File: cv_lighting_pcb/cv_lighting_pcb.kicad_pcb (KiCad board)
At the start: 2 copper layers, 83.8 x 78.7 mm, 27 parts, among them Q1 2N3906, U1 Current Driver, U2 Camera Input, U3 VO617A, U4 Barrel Jack

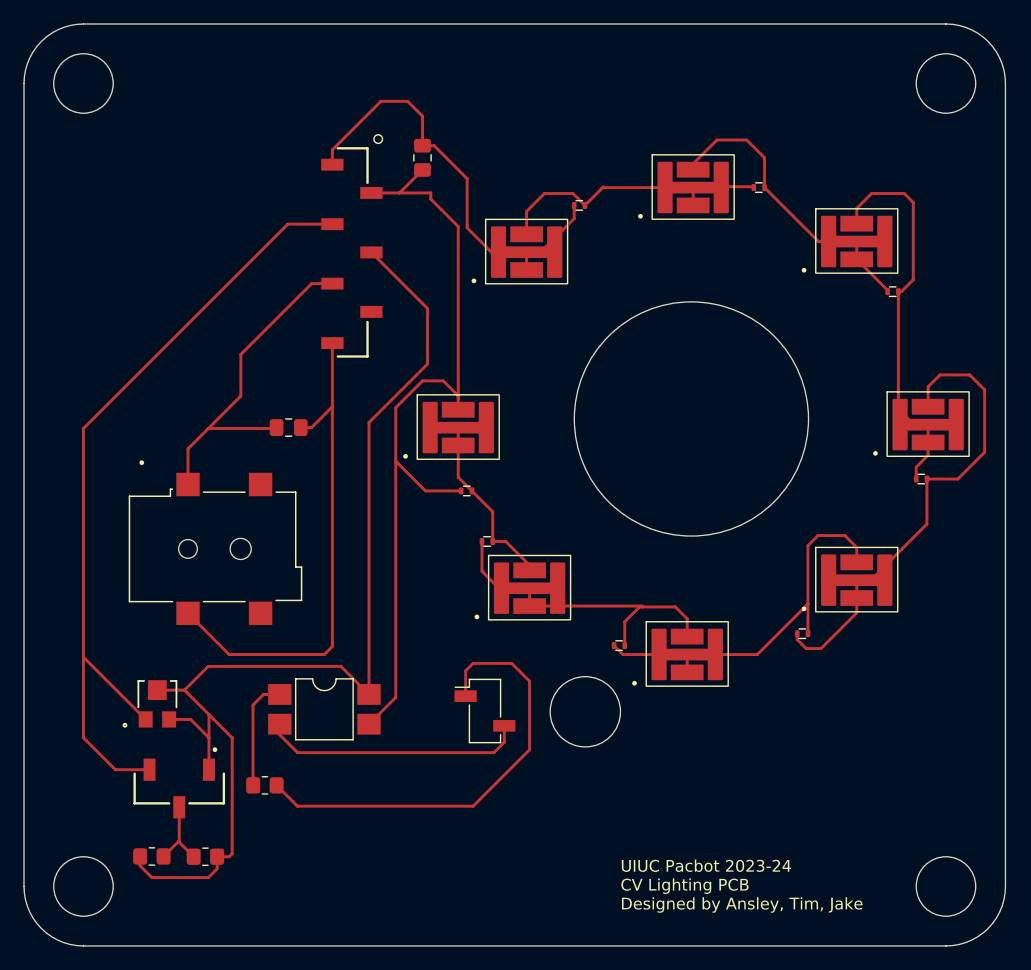
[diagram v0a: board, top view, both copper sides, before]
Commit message: more changes to lighting pcb
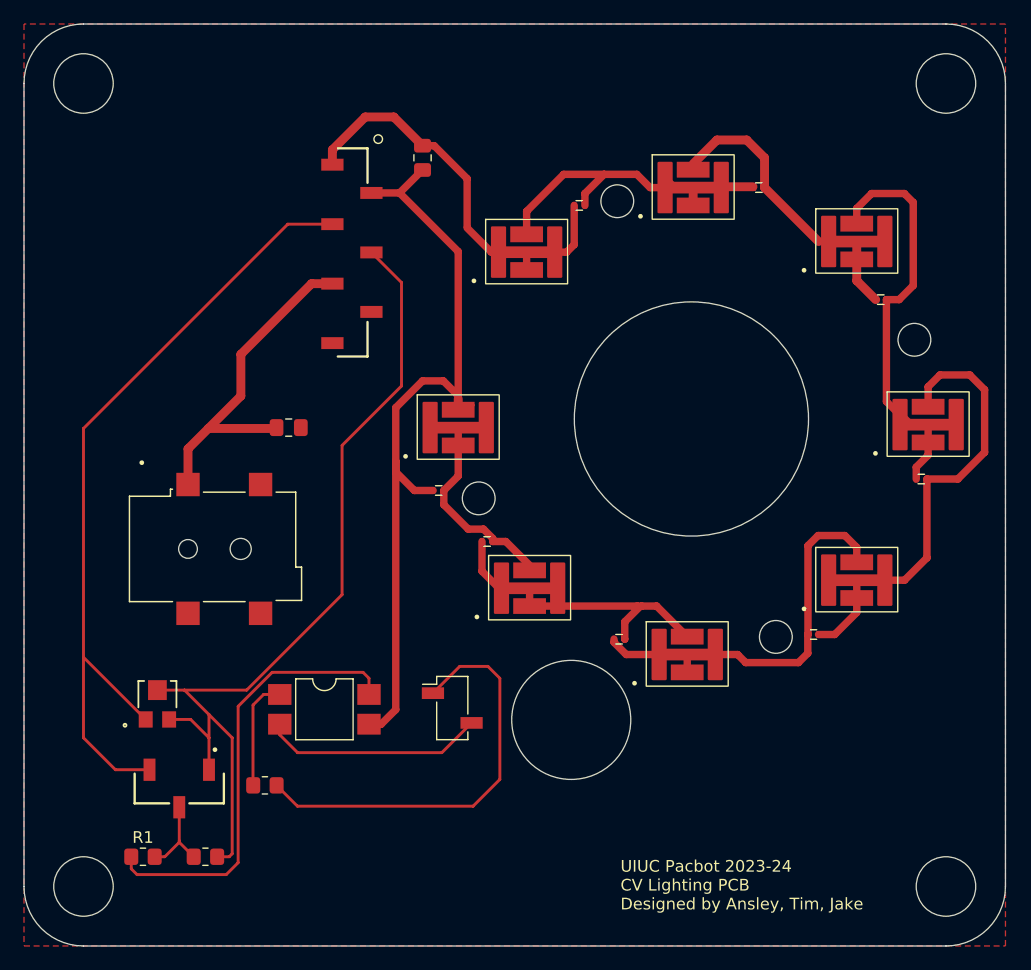
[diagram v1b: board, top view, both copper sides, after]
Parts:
- R3: value 1K -> 200
- moved D12 7.94 mm to (166.5, 104.3), turned to 180 degrees
- moved U2 2.81 mm to (135.6, 106.7)
- moved D15 2.40 mm to (134.5, 92.0)
- moved D10 1.23 mm to (172.3, 67.9)
- moved R1 0.76 mm to (109.2, 119.4)
- moved D13 0.55 mm to (149.9, 96.9)
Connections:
- R1 pad 1: Net-(Q1-E) -> Net-(R1-Pad1)
- U3 pad 4: Net-(Q1-E) -> Net-(R1-Pad1)
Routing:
- net GND: track 43.4 -> 0.00 mm
- net Net-(R1-Pad1): track 0.00 -> 38.1 mm
- net Net-(Q1-E): track 96.7 -> 77.4 mm
- net Net-(D1-K): track 24.3 -> 30.4 mm
- net Net-(U2-PWM_GND): track 22.5 -> 19.0 mm
- net Net-(D10-A): track 33.4 -> 36.9 mm
- net Net-(U2-PWM_Input): track 38.7 -> 36.5 mm
- net Net-(D15-A): track 70.7 -> 68.8 mm
- net Net-(D14-A): track 15.4 -> 17.1 mm
- net Net-(D13-A): track 28.2 -> 27.2 mm
- net Net-(D12-A): track 33.9 -> 34.8 mm
- net Net-(Q1-B): track 6.63 -> 7.35 mm
- added copper zone on F.Cu, net GND
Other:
- outline, holes or cut-outs redrawn

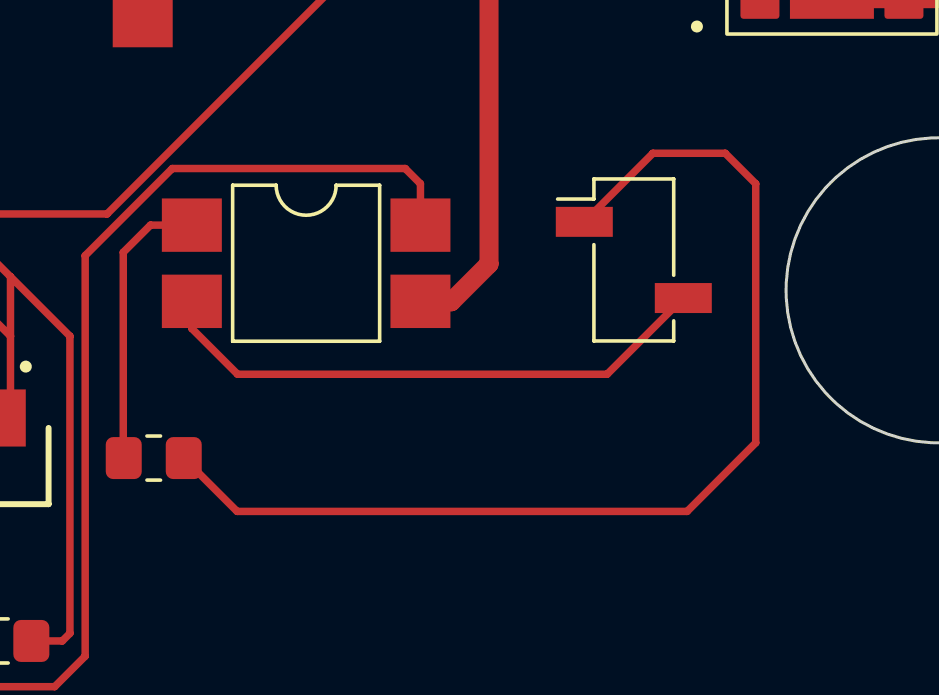
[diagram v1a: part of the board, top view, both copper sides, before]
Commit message: more changes to lighting pcb
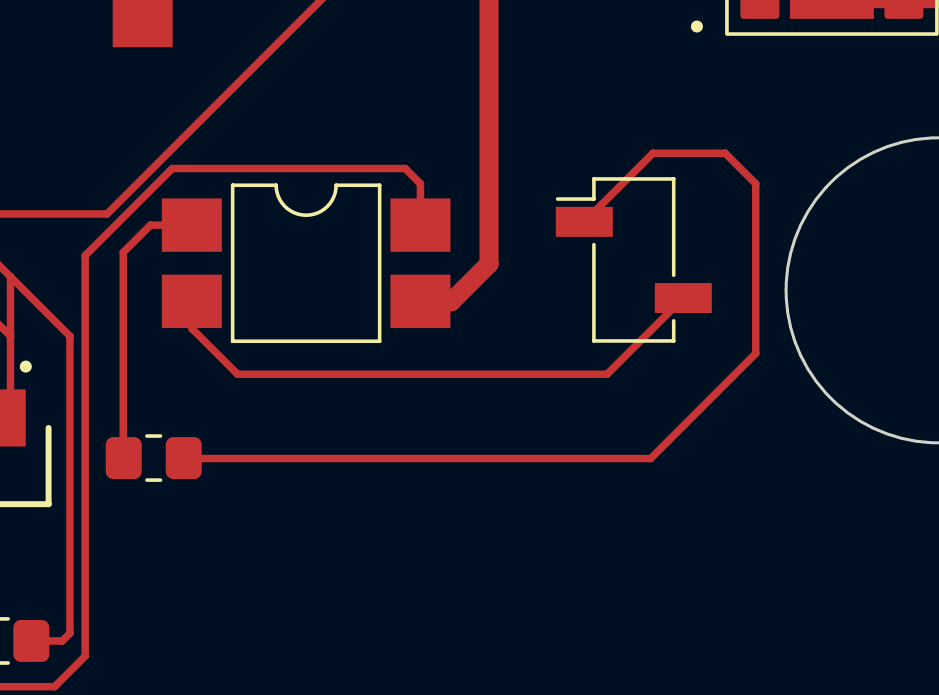
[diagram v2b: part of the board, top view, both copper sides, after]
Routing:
- net Net-(U2-PWM_Input): track 36.5 -> 33.3 mm
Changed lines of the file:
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@@
     (effects (font (size 1 1) (thickness 0.15)) (justify left bottom))
   )
-  (gr_text "hole for wire from camera to pcb\n\n" (at 149.86 116.332) (layer "F.Fab")
+  (gr_text "hole for wire from camera to pcb\n\n" (at 141.9 116.4) (layer "F.Fab")
     (effects (font (size 1 1) (thickness 0.15)) (justify left bottom))
   )
@@
   (segment (start 118.618 113.268) (end 118.634 113.284) (width 0.25) (layer "F.Cu") (net 14))
   (segment (start 119.5245 105.5195) (end 118.618 106.426) (width 0.25) (layer "F.Cu") (net 14))
-  (segment (start 139.7 112.776) (end 137.414 115.062) (width 0.25) (layer "F.Cu") (net 15))
-  (segment (start 139.7 104.14) (end 139.7 112.776) (width 0.25) (layer "F.Cu") (net 15))
   (segment (start 138.684 103.124) (end 139.7 104.14) (width 0.25) (layer "F.Cu") (net 15))
+  (segment (start 136.2 113.3) (end 120.65 113.3) (width 0.25) (layer "F.Cu") (net 15))
+  (segment (start 120.65 113.3) (end 120.634 113.284) (width 0.25) (layer "F.Cu") (net 15))
+  (segment (start 139.7 109.8) (end 136.2 113.3) (width 0.25) (layer "F.Cu") (net 15))
+  (segment (start 139.7 104.14) (end 139.7 109.8) (width 0.25) (layer "F.Cu") (net 15))
+  (segment (start 133.986 105.41) (end 136.272 103.124) (width 0.25) (layer "F.Cu") (net 15))
   (segment (start 136.272 103.124) (end 138.684 103.124) (width 0.25) (layer "F.Cu") (net 15))
-  (segment (start 137.414 115.062) (end 122.412 115.062) (width 0.25) (layer "F.Cu") (net 15))
-  (segment (start 133.986 105.41) (end 136.272 103.124) (width 0.25) (layer "F.Cu") (net 15))
-  (segment (start 122.412 115.062) (end 120.634 113.284) (width 0.25) (layer "F.Cu") (net 15))
   (segment (start 120.904 108.966) (end 122.428 110.49) (width 0.25) (layer "F.Cu") (net 17))
   (segment (start 120.904 108.0595) (end 120.904 108.966) (width 0.25) (layer "F.Cu") (net 17))

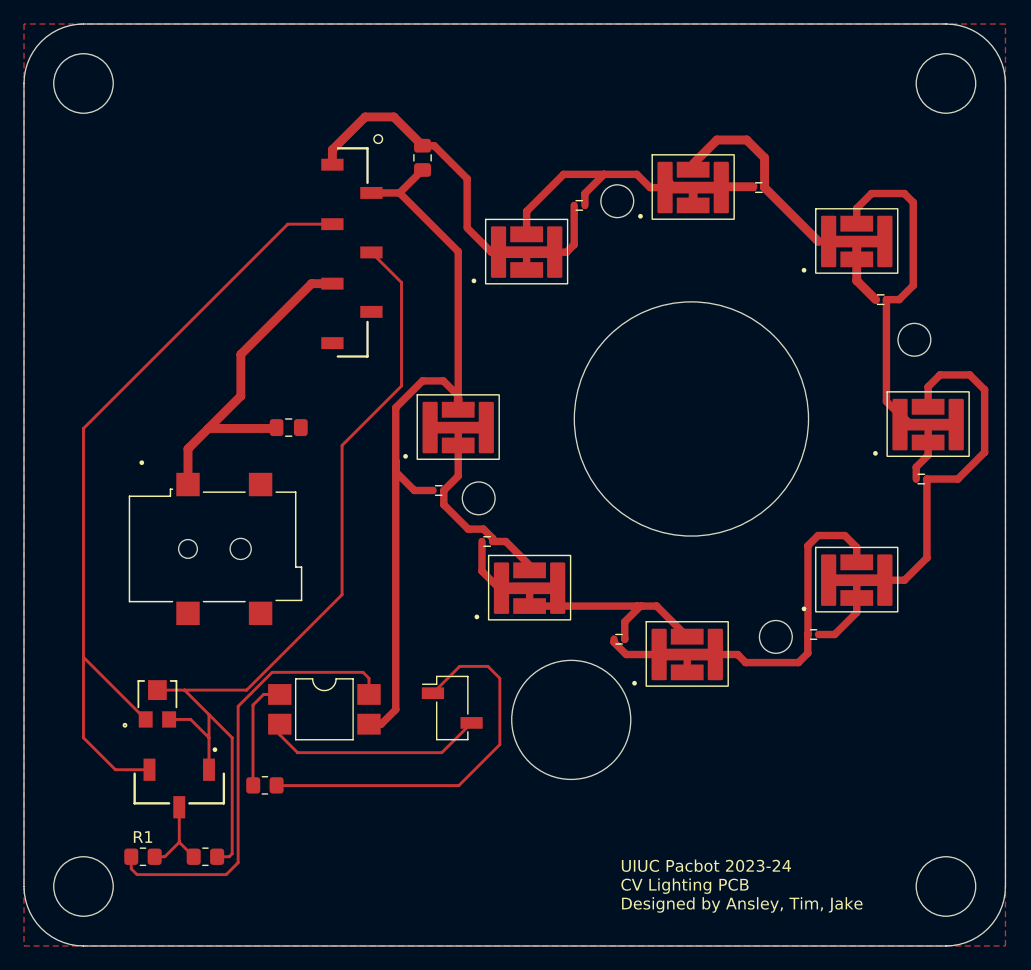
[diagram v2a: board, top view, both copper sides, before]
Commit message: more changes to lighting pcb
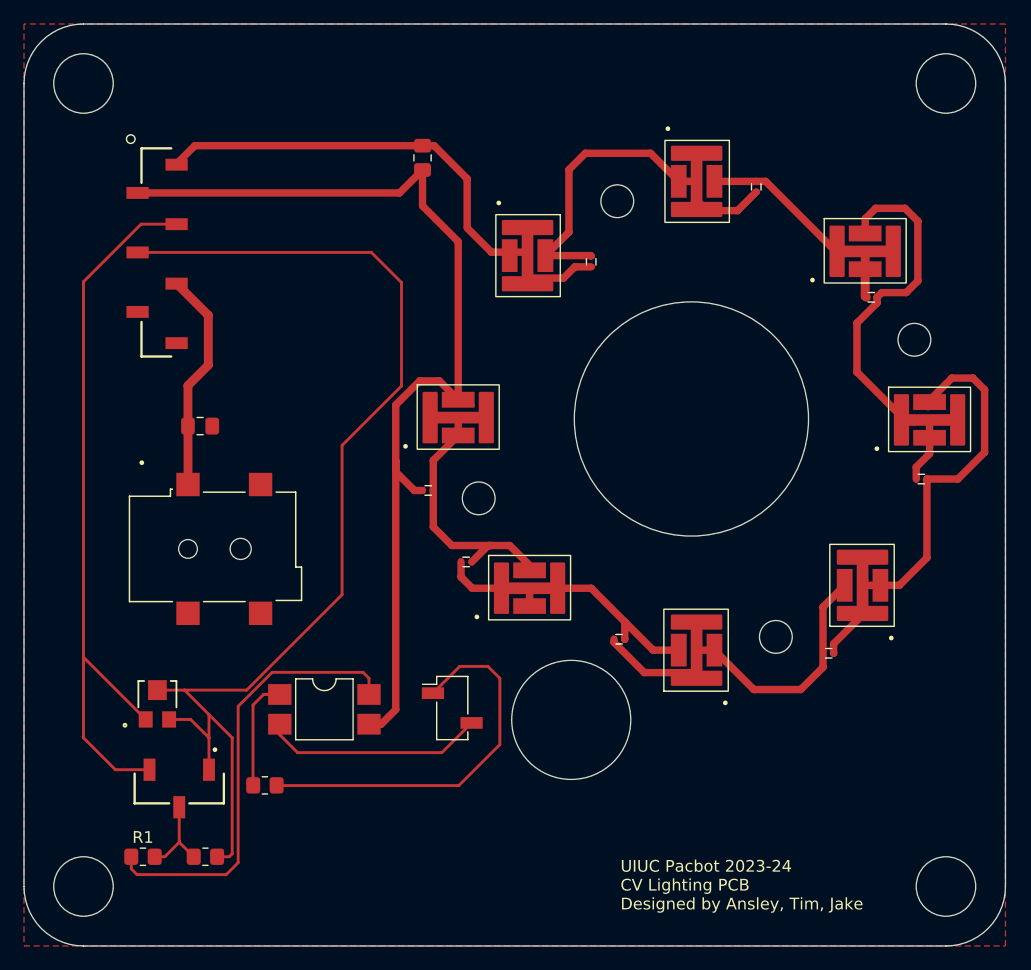
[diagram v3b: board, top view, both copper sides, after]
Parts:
- moved D17 9.18 mm to (143.6, 68.5), turned to 90 degrees
- moved C1 7.57 mm to (114.1, 82.6)
- moved D9 5.65 mm to (157.7, 62.1), turned to 90 degrees
- moved D14 2.50 mm to (136.8, 90.3)
- moved D12 2.06 mm to (167.8, 105.9)
- moved D1 1.40 mm to (142.9, 68.0), turned to -90 degrees
- moved D5 1.27 mm to (169.9, 96.2), turned to 90 degrees
- moved D2 1.12 mm to (157.3, 61.7), turned to -90 degrees
- moved D3 1.10 mm to (170.9, 66.9)
- moved D15 0.90 mm to (133.6, 92.0)
- moved D8 0.85 mm to (136.1, 81.1)
- moved D10 0.82 mm to (171.5, 67.7)
- moved D6 0.43 mm to (155.7, 101.7), turned to 90 degrees
- moved D4 0.42 mm to (176.4, 81.3)
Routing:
- net Net-(Q1-E): track 77.4 -> 97.3 mm
- net Net-(D15-A): track 68.8 -> 87.4 mm
- net +30V: track 29.2 -> 19.0 mm
- net Net-(D1-A): track 36.7 -> 46.8 mm
- net Net-(D10-K): track 27.8 -> 19.3 mm
- net Net-(Q1-C): track 69.2 -> 63.2 mm
- net Net-(D14-A): track 17.1 -> 22.5 mm
- net Net-(D12-A): track 34.8 -> 32.4 mm
- net Net-(D1-K): track 30.4 -> 32.6 mm
- net Net-(D11-A): track 40.2 -> 42.3 mm
- net Net-(D13-A): track 27.2 -> 25.5 mm
- net Net-(D10-A): track 36.9 -> 38.2 mm

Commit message: more changes to cv lighting
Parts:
- removed Q1: 2N3906, cv_lighting_footprints:2N3906
- removed R1: 5K, Resistor_SMD:R_0805_2012Metric_Pad1.20x1.40mm_HandSolder
- removed R3: 200, Resistor_SMD:R_0805_2012Metric_Pad1.20x1.40mm_HandSolder
- removed U3: VO617A, cv_lighting_footprints:VO617A
- added Q2: MMBT3904, cv_lighting_footprints:MMBT3904, F.Cu at (126.0, 102.6)
- moved R2 14.2 mm to (120.7, 106.6)
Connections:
- R2 pad 1: Net-(Q1-B) -> Net-(Q2-B)
- U2 pad 1: Net-(U2-PWM_Input) -> Net-(Q2-B)
- U2 pad 2: Net-(U2-PWM_GND) -> Net-(D15-A)
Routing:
- net Net-(R1-Pad1): track 38.1 -> 0.00 mm
- net Net-(U2-PWM_Input): track 33.3 -> 0.00 mm
- net Net-(U2-PWM_GND): track 19.0 -> 0.00 mm
- net Net-(Q2-B): track 0.00 -> 16.4 mm
- net Net-(Q2-E): track 63.2 -> 78.1 mm
- net Net-(R3-Pad2): track 9.53 -> 0.00 mm
- net Net-(Q2-C): track 97.3 -> 88.6 mm
- net Net-(Q1-B): track 7.35 -> 0.00 mm
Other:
- board size 83.8 x 78.7 mm -> 83.8 x 68.6 mm

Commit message: changes to cv lighting
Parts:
- renumbered R2 to R1
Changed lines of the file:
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@@
     (property "ki_keywords" "R res resistor")
     (attr smd)
-    (fp_text reference "R2" (at 0 -1.65) (layer "F.Fab")
+    (fp_text reference "R1" (at 0 -1.65) (layer "F.Fab")
         (effects (font (size 1 1) (thickness 0.15)))
     )

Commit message: more changes to cv lighting for like the 100th time
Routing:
- net Net-(Q2-C): track 88.6 -> 73.6 mm
- net Net-(Q2-E): track 78.1 -> 79.1 mm
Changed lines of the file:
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@@
   (segment (start 136.144 83.4) (end 136.144 81.8782) (width 0.635) (layer "F.Cu") (net 8))
   (segment (start 135.6 92.8) (end 138.9464 92.8) (width 0.635) (layer "F.Cu") (net 8))
-  (segment (start 130.81 95.41) (end 138 102.6) (width 0.635) (layer "F.Cu") (net 9))
   (segment (start 136.144 80.35) (end 134.534 78.74) (width 0.635) (layer "F.Cu") (net 9))
   (segment (start 132.86 78.74) (end 130.81 80.79) (width 0.635) (layer "F.Cu") (net 9))
@@
   (segment (start 133.096 60.7275) (end 131.136 62.6875) (width 0.635) (layer "F.Cu") (net 9))
   (segment (start 132.4 88.1) (end 133.1 88.1) (width 0.635) (layer "F.Cu") (net 9))
+  (segment (start 137.922 107.314) (end 137.286 107.95) (width 0.635) (layer "F.Cu") (net 9))
   (segment (start 133.096 60.7275) (end 133.096 63.796) (width 0.635) (layer "F.Cu") (net 9))
   (segment (start 130.81 80.79) (end 130.81 85.598) (width 0.635) (layer "F.Cu") (net 9))
-  (segment (start 138 107.236) (end 137.286 107.95) (width 0.635) (layer "F.Cu") (net 9))
-  (segment (start 130.81 86.51) (end 130.81 95.41) (width 0.635) (layer "F.Cu") (net 9))
   (segment (start 130.81 85.598) (end 130.81 86.51) (width 0.635) (layer "F.Cu") (net 9))
   (segment (start 136.144 80.35) (end 136.144 80.264) (width 0.762) (layer "F.Cu") (net 9))
   (segment (start 137.45 80.808) (end 136.144 80.808) (width 0.25) (layer "F.Cu") (net 9))
+  (segment (start 137.922 102.522) (end 137.922 107.314) (width 0.635) (layer "F.Cu") (net 9))
+  (segment (start 130.81 95.41) (end 137.922 102.522) (width 0.635) (layer "F.Cu") (net 9))
   (segment (start 130.81 86.51) (end 132.4 88.1) (width 0.635) (layer "F.Cu") (net 9))
   (segment (start 134.534 78.74) (end 132.86 78.74) (width 0.635) (layer "F.Cu") (net 9))
   (segment (start 133.096 63.796) (end 136.144 66.844) (width 0.635) (layer "F.Cu") (net 9))
-  (segment (start 138 102.6) (end 138 107.236) (width 0.635) (layer "F.Cu") (net 9))
+  (segment (start 130.81 86.51) (end 130.81 95.41) (width 0.635) (layer "F.Cu") (net 9))
   (segment (start 113.0625 79.1375) (end 114.8 77.4) (width 0.762) (layer "F.Cu") (net 10))
   (segment (start 113.0625 82.6) (end 113.0625 79.1375) (width 0.762) (layer "F.Cu") (net 10))
@@
   (segment (start 113.066 87.591) (end 113.066 82.6035) (width 0.762) (layer "F.Cu") (net 10))
   (segment (start 113.066 82.6035) (end 113.0625 82.6) (width 0.762) (layer "F.Cu") (net 10))
+  (segment (start 104.14 102.340551) (end 104.14 68.58) (width 0.25) (layer "F.Cu") (net 14))
   (segment (start 104.14 102.340551) (end 109.453549 107.6541) (width 0.25) (layer "F.Cu") (net 14))
+  (segment (start 104.14 68.58) (end 107.3655 65.3545) (width 0.25) (layer "F.Cu") (net 14))
   (segment (start 107.4 109.6) (end 104.14 106.34) (width 0.25) (layer "F.Cu") (net 14))
   (segment (start 104.14 106.34) (end 104.14 102.340551) (width 0.25) (layer "F.Cu") (net 14))
-  (segment (start 104.14 70.2755) (end 109.061 65.3545) (width 0.25) (layer "F.Cu") (net 14))
+  (segment (start 107.3655 65.3545) (end 112.0925 65.3545) (width 0.25) (layer "F.Cu") (net 14))
   (segment (start 125.9 109.6) (end 107.4 109.6) (width 0.25) (layer "F.Cu") (net 14))
   (segment (start 126.9 108.6) (end 125.9 109.6) (width 0.25) (layer "F.Cu") (net 14))
-  (segment (start 109.061 65.3545) (end 112.0925 65.3545) (width 0.25) (layer "F.Cu") (net 14))
-  (segment (start 104.14 102.340551) (end 104.14 70.2755) (width 0.25) (layer "F.Cu") (net 14))
-  (segment (start 125.828249 108.6) (end 129.018249 105.41) (width 0.25) (layer "F.Cu") (net 15))
-  (segment (start 129.018249 105.41) (end 133.986 105.41) (width 0.25) (layer "F.Cu") (net 15))
+  (segment (start 128.898125 105.41) (end 133.986 105.41) (width 0.25) (layer "F.Cu") (net 15))
+  (segment (start 125 108.6) (end 125.708125 108.6) (width 0.25) (layer "F.Cu") (net 15))
   (segment (start 125 108.6) (end 121.7 108.6) (width 0.25) (layer "F.Cu") (net 15))
-  (segment (start 125 108.6) (end 125.828249 108.6) (width 0.25) (layer "F.Cu") (net 15))
+  (segment (start 125.708125 108.6) (end 128.898125 105.41) (width 0.25) (layer "F.Cu") (net 15))
   (segment (start 121.7 108.6) (end 119.7 106.6) (width 0.25) (layer "F.Cu") (net 15))
   (segment (start 110.45355 105.1471) (end 112.7671 105.1471) (width 0.25) (layer "F.Cu") (net 16))
   (segment (start 111.453551 107.6541) (end 115.5709 107.6541) (width 0.25) (layer "F.Cu") (net 16))
-  (segment (start 131.3 70.338) (end 131.3 79.175) (width 0.25) (layer "F.Cu") (net 16))
+  (segment (start 108.7605 67.7675) (end 113.4875 67.7675) (width 0.25) (layer "F.Cu") (net 16))
   (segment (start 121.7 106.6) (end 121.7 101.525) (width 0.25) (layer "F.Cu") (net 16))
   (segment (start 125.95 106.58) (end 121.72 106.58) (width 0.25) (layer "F.Cu") (net 16))
-  (segment (start 126.225 84.25) (end 126.225 97) (width 0.25) (layer "F.Cu") (net 16))
+  (segment (start 123.952 78.232) (end 123.952 99.273) (width 0.25) (layer "F.Cu") (net 16))
   (segment (start 118.0779 105.1471) (end 112.7671 105.1471) (width 0.25) (layer "F.Cu") (net 16))
-  (segment (start 131.3 70.338) (end 128.7295 67.7675) (width 0.25) (layer "F.Cu") (net 16))
   (segment (start 121.7625 101.4625) (end 118.0779 105.1471) (width 0.25) (layer "F.Cu") (net 16))
-  (segment (start 126.225 97) (end 121.7625 101.4625) (width 0.25) (layer "F.Cu") (net 16))
-  (segment (start 131.3 79.175) (end 126.225 84.25) (width 0.25) (layer "F.Cu") (net 16))
-  (segment (start 128.7295 67.7675) (end 108.7605 67.7675) (width 0.25) (layer "F.Cu") (net 16))
   (segment (start 121.7 101.525) (end 121.7625 101.4625) (width 0.25) (layer "F.Cu") (net 16))
   (segment (start 121.72 106.58) (end 121.7 106.6) (width 0.25) (layer "F.Cu") (net 16))
+  (segment (start 123.952 99.273) (end 121.7625 101.4625) (width 0.25) (layer "F.Cu") (net 16))
   (segment (start 115.5709 107.6541) (end 118.0779 105.1471) (width 0.25) (layer "F.Cu") (net 16))
+  (segment (start 113.4875 67.7675) (end 123.952 78.232) (width 0.25) (layer "F.Cu") (net 16))
   (zone (net 11) (net_name "GND") (layer "F.Cu") (hatch edge 0.5)
     (connect_pads (clearance 0.5))
     (min_thickness 0.25) (filled_areas_thickness no)
-    (fill yes (thermal_gap 0.5) (thermal_bridge_width 0.5) (island_removal_mode 1) (island_area_min 9.999999))
+    (fill yes (thermal_gap 0.5) (thermal_bridge_width 0.5) (island_removal_mode 1) (island_area_min 9.999998))
     (polygon
       (pts
